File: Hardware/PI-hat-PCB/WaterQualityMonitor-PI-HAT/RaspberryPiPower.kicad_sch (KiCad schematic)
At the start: 19 parts

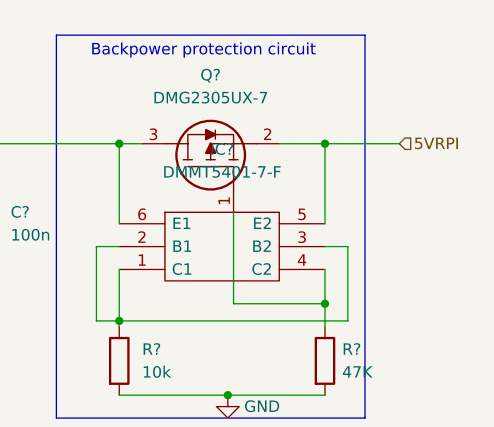
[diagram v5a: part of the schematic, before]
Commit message: Updated designs
changed some labels to correct ones (glob, hier, net, input, output)
added H-bridge to peltier for cooling and heating functionality
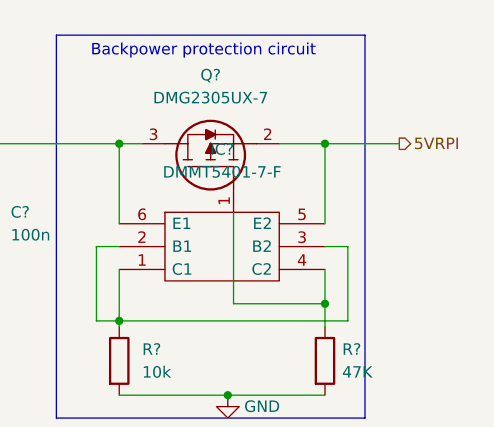
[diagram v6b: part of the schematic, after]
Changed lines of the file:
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@@
     (effects (font (size 1.27 1.27)) (justify left bottom))
   )
-  (hierarchical_label "5VRPI" (shape input) (at 254 93.98 0)
+  (hierarchical_label "5VRPI" (shape output) (at 254 93.98 0)
     (effects (font (size 1.27 1.27)) (justify left))
   )
@@
   (symbol (lib_id "power:GND") (at 234.95 121.92 0) (unit 1)
     (in_bom yes) (on_board yes)
-    (property "Reference" "#PWR?" (id 0) (at 234.95 128.27 0)
+    (property "Reference" "#PWR0116" (id 0) (at 234.95 128.27 0)
       (effects (font (size 1.27 1.27)) hide)
     )
@@
   (symbol (lib_id "power:GND") (at 179.07 120.65 0) (unit 1)
     (in_bom yes) (on_board yes) (fields_autoplaced)
-    (property "Reference" "#PWR?" (id 0) (at 179.07 127 0)
+    (property "Reference" "#PWR0119" (id 0) (at 179.07 127 0)
       (effects (font (size 1.27 1.27)) hide)
     )
@@
   (symbol (lib_id "power:GND") (at 121.92 105.41 0) (unit 1)
     (in_bom yes) (on_board yes) (fields_autoplaced)
-    (property "Reference" "#PWR?" (id 0) (at 121.92 111.76 0)
+    (property "Reference" "#PWR0115" (id 0) (at 121.92 111.76 0)
       (effects (font (size 1.27 1.27)) hide)
     )
@@
   (symbol (lib_id "power:GND") (at 152.4 125.73 0) (unit 1)
     (in_bom yes) (on_board yes) (fields_autoplaced)
-    (property "Reference" "#PWR?" (id 0) (at 152.4 132.08 0)
+    (property "Reference" "#PWR0118" (id 0) (at 152.4 132.08 0)
       (effects (font (size 1.27 1.27)) hide)
     )
@@
   (symbol (lib_id "power:GND") (at 115.57 114.3 0) (unit 1)
     (in_bom yes) (on_board yes) (fields_autoplaced)
-    (property "Reference" "#PWR?" (id 0) (at 115.57 120.65 0)
-      (effects (font (size 1.27 1.27)) hide)
-    )
+    (property "Reference" "#PWR0117" (id 0) (at 115.57 120.65 0)
+      (effects (font (size 1.27 1.27)) hide)
+    )

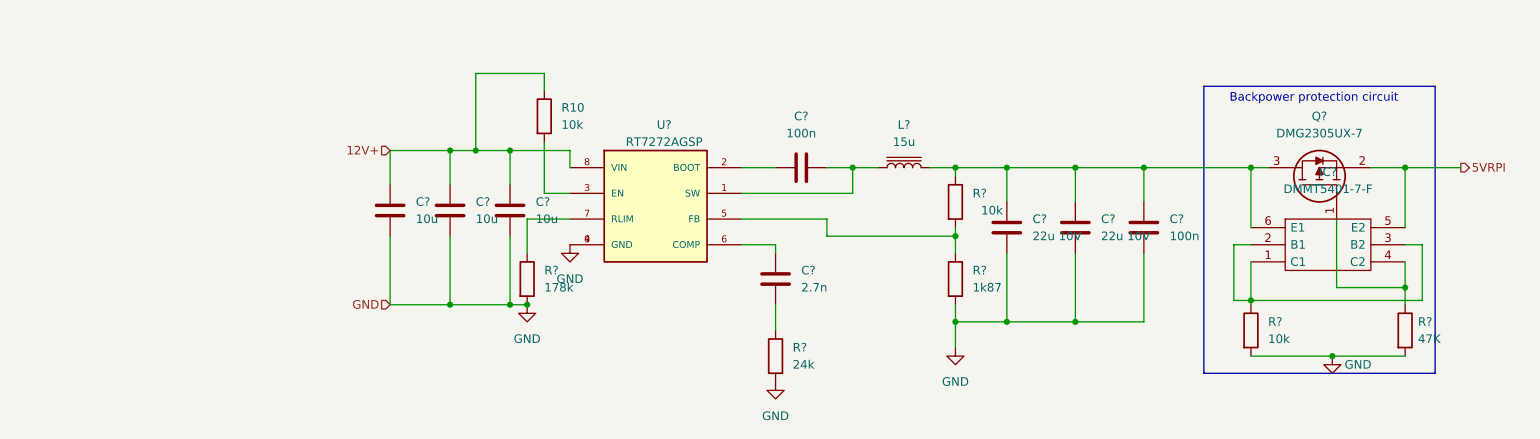
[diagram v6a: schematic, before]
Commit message: assigent footprints to all current components
I chose 1206smd handsolderable for caps and resistors and inductors, may need to be revised
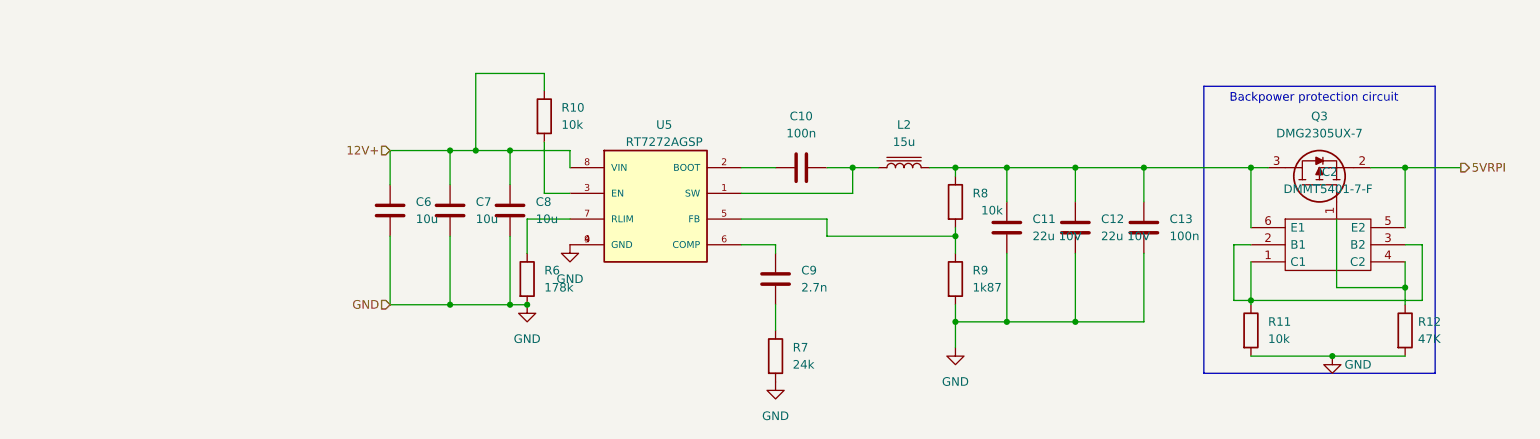
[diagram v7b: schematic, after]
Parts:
- C10, C11, C12, C13, C6, C7, C8, C9: renamed from C?; footprint (none) -> Capacitor_SMD:C_1206_3216Metric_Pad1.33x1.80mm_HandSolder
- IC2: renamed from IC?; footprint SOT95P285X140-6N -> SmacSYs:SOT95P285X140-6N
- L2: renamed from L?; footprint (none) -> Inductor_SMD:L_1206_3216Metric_Pad1.22x1.90mm_HandSolder
- Q3: renamed from Q?; footprint SOT96P240X110-3N -> Snapeda:SOT91P240X110-3N_DMG2305UX-7
- R10: footprint (none) -> Resistor_SMD:R_1206_3216Metric_Pad1.30x1.75mm_HandSolder
- R11, R12, R6, R7, R8, R9: renamed from R?; footprint (none) -> Resistor_SMD:R_1206_3216Metric_Pad1.30x1.75mm_HandSolder
- U5: renamed from U?; footprint SOIC127P599X175-9N -> Snapeda:SOIC127P599X175-9N
